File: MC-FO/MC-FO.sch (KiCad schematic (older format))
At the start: 16 parts, among them J1 86094327313755E1LF, U161 IFD97, U163 74LVC1G32SE-7

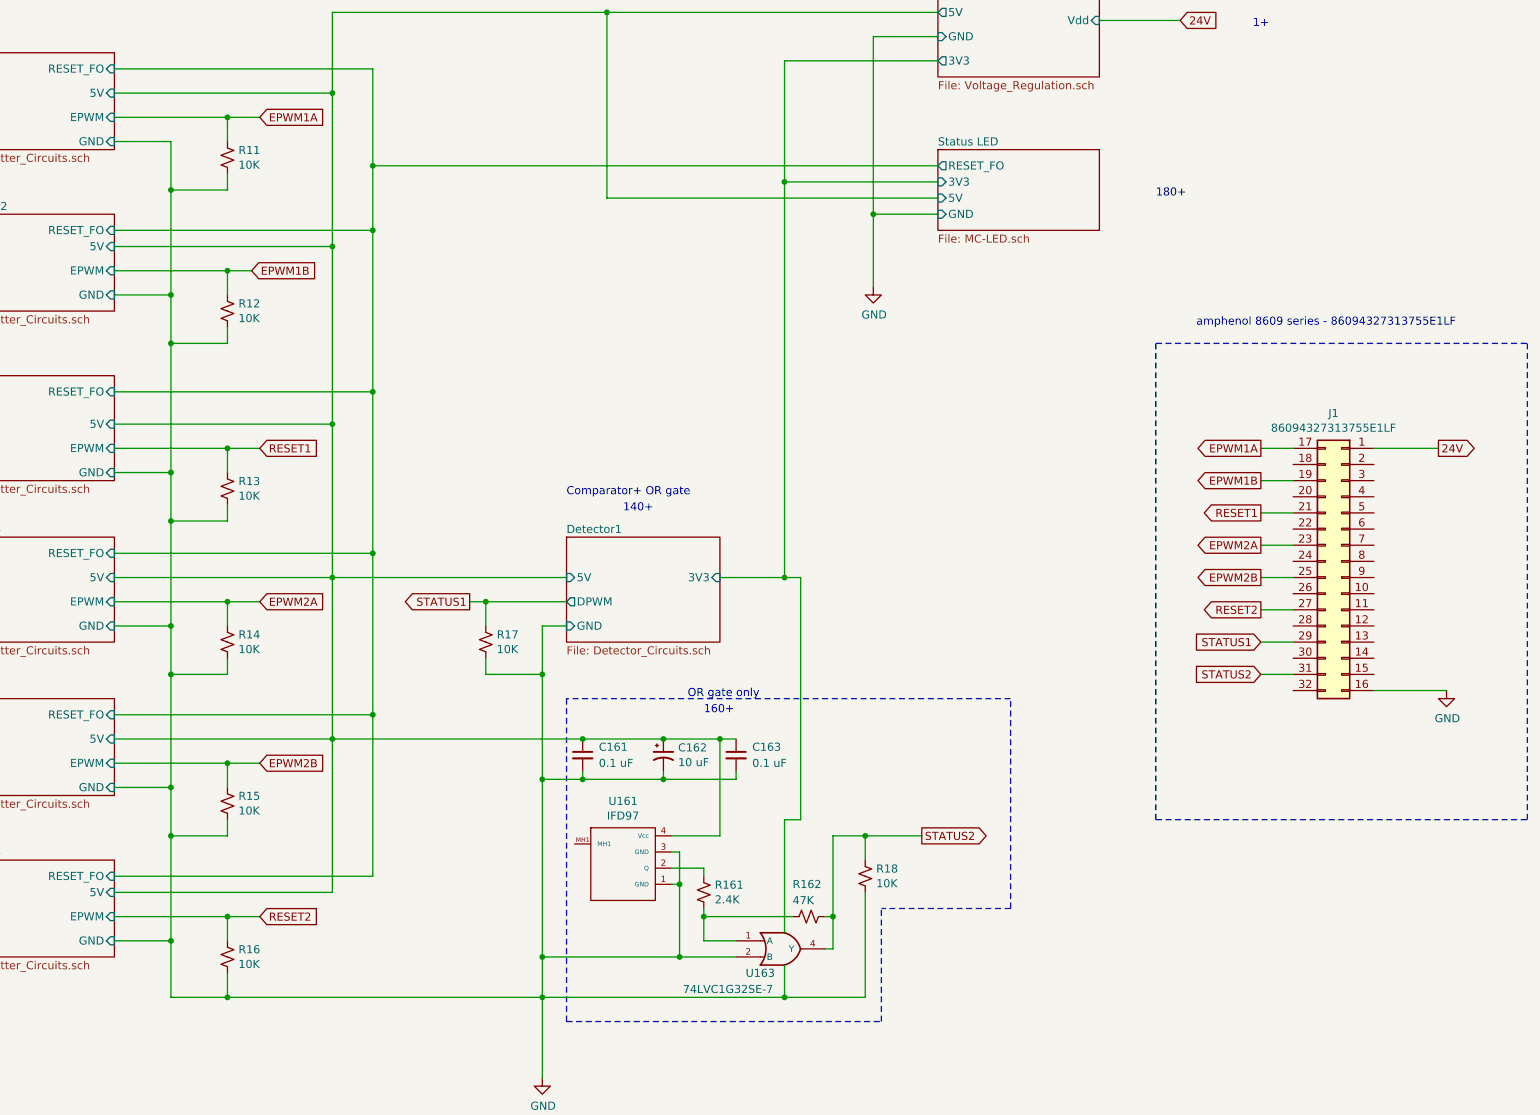
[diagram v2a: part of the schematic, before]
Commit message: DSP schem, FO schem, and FO layout changes
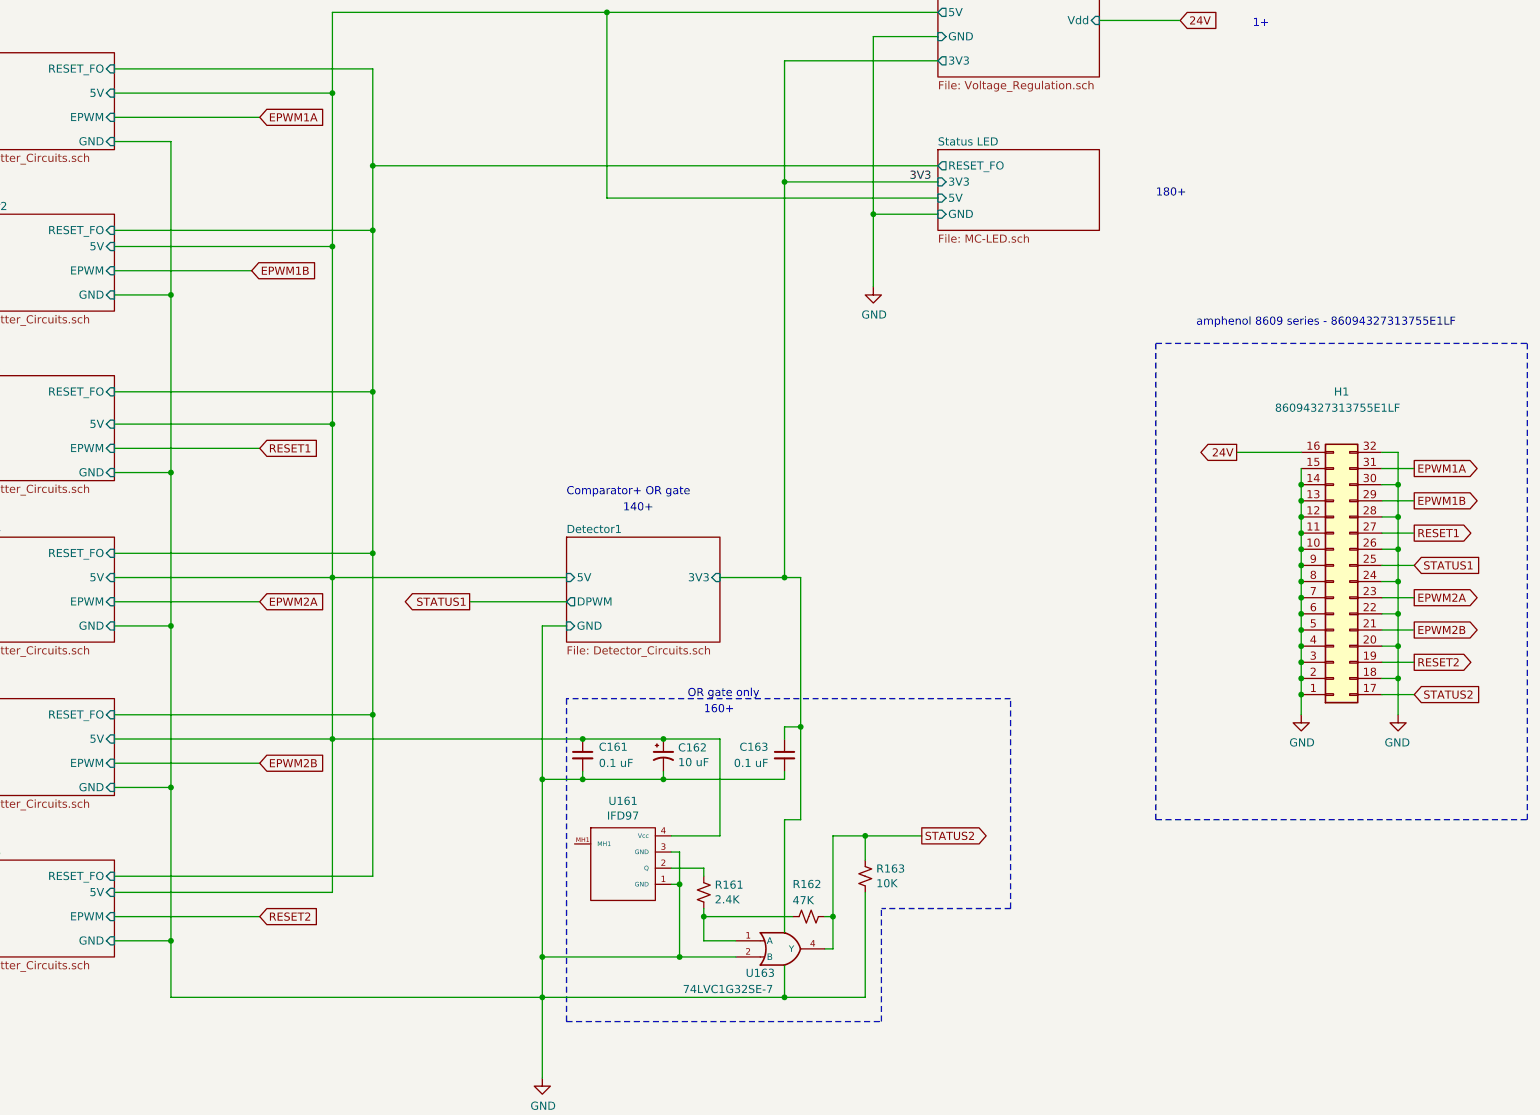
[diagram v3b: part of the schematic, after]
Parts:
- removed R11, R12, R13, R14, R15, R16, R17: 10K, Resistor_SMD:R_0603_1608Metric, symbol Device:R_Small_US
- renumbered J1 to H1, R18 to R163
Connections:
- net 24V: now also H1.16 (Pin_16); no longer H1.1 (Pin_1)
- net Detector1/5V: no longer C163.1
- net EPWM1A: now also H1.31 (Pin_31); no longer H1.17 (Pin_17)
- net EPWM1B: now also H1.29 (Pin_29); no longer H1.19 (Pin_19)
- net EPWM2B: now also H1.21 (Pin_21); no longer H1.25 (Pin_25)
- net GND: now also H1.1 (Pin_1), H1.10 (Pin_10), H1.11 (Pin_11), H1.12 (Pin_12), H1.13 (Pin_13), H1.14 (Pin_14), H1.15 (Pin_15), H1.18 (Pin_18), H1.2 (Pin_2), H1.20 (Pin_20), H1.22 (Pin_22), H1.24 (Pin_24), H1.26 (Pin_26), H1.28 (Pin_28), H1.3 (Pin_3), H1.30 (Pin_30), H1.32 (Pin_32), H1.4 (Pin_4), H1.5 (Pin_5), H1.6 (Pin_6), H1.7 (Pin_7), H1.8 (Pin_8), H1.9 (Pin_9); no longer H1.16 (Pin_16)
- net RESET1: now also H1.27 (Pin_27); no longer H1.21 (Pin_21)
- net RESET2: now also H1.19 (Pin_19); no longer H1.27 (Pin_27)
- net STATUS1: now also H1.25 (Pin_25); no longer H1.29 (Pin_29)
- net STATUS2: now also H1.17 (Pin_17); no longer H1.31 (Pin_31)
- net VCC: now also C163.1
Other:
- moved on the sheet: C163, H1

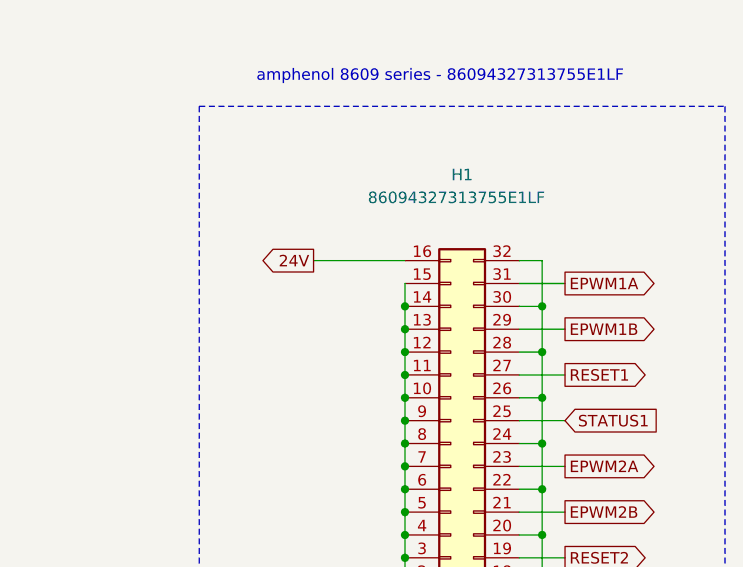
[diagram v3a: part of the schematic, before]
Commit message: Routed FO schematic
All FO circuits routed except LED and Detector circuits.
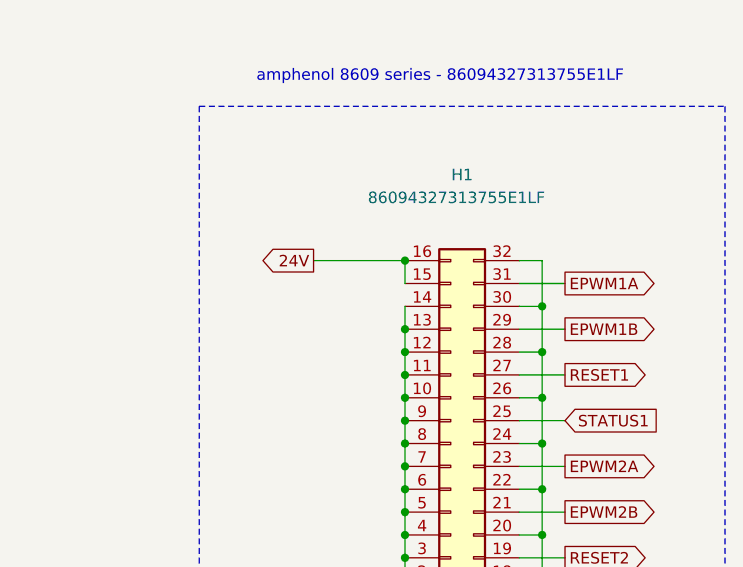
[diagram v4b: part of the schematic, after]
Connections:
- net 24V: now also H1.15 (Pin_15)
- net GND: no longer H1.15 (Pin_15)
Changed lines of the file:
@@
 EPWM1A
 Connection ~ 10000 4975
-Connection ~ 9400 4275
-Wire Wire Line
-	9400 4375 9400 4275
-Connection ~ 9400 4375
-Wire Wire Line
-	9400 4475 9400 4375
-Connection ~ 9400 4475
-Wire Wire Line
-	9400 4575 9400 4475
-Connection ~ 9400 4575
-Wire Wire Line
-	9400 4675 9400 4575
-Connection ~ 9400 4675
-Wire Wire Line
-	9400 4775 9400 4675
-Connection ~ 9400 4775
-Wire Wire Line
-	9400 4875 9400 4775
-Connection ~ 9400 4875
-Wire Wire Line
-	9400 4975 9400 4875
-Connection ~ 9400 4975
-Wire Wire Line
-	9400 3775 9400 3875
-Connection ~ 9400 3875
-Wire Wire Line
-	9400 3975 9400 3875
-Connection ~ 9400 3975
-Wire Wire Line
-	9400 4075 9400 3975
-Connection ~ 9400 4075
-Wire Wire Line
-	9400 4275 9400 4175
-Wire Wire Line
-	9400 4175 9400 4075
-Connection ~ 9400 4175
-Wire Wire Line
-	9400 5075 9400 5200
-Wire Wire Line
-	9400 4975 9400 5075
-Connection ~ 9400 5075
-$Comp
-L Existing_IC_Models:86094327313755E1LF H1
-U 1 1 61916120
-P 9600 4375
-F 0 "H1" H 9650 3200 50  0000 C CNN
-F 1 "86094327313755E1LF" H 9625 3300 50  0000 C CNN
-F 2 "Footprints_MC-FO:86094327313755E1LF" H 9600 4375 50  0001 C CNN
-F 3 "~" H 9600 4375 50  0001 C CNN
-	1    9600 4375
-	1    0    0    1
-$EndComp
-Wire Wire Line
-	9400 3775 9400 3675
-Connection ~ 9400 3775
 Wire Wire Line
 	10000 3575 9900 3575
@@
 Wire Wire Line
 	4250 4500 4850 4500
+Connection ~ 9400 4275
+Wire Wire Line
+	9400 4375 9400 4275
+Connection ~ 9400 4375
+Wire Wire Line
+	9400 4475 9400 4375
+Connection ~ 9400 4475
+Wire Wire Line
+	9400 4575 9400 4475
+Connection ~ 9400 4575
+Wire Wire Line
+	9400 4675 9400 4575
+Connection ~ 9400 4675
+Wire Wire Line
+	9400 4775 9400 4675
+Connection ~ 9400 4775
+Wire Wire Line
+	9400 4875 9400 4775
+Connection ~ 9400 4875
+Wire Wire Line
+	9400 4975 9400 4875
+Connection ~ 9400 4975
+Wire Wire Line
+	9400 3775 9400 3875
+Connection ~ 9400 3875
+Wire Wire Line
+	9400 3975 9400 3875
+Connection ~ 9400 3975
+Wire Wire Line
+	9400 4075 9400 3975
+Connection ~ 9400 4075
+Wire Wire Line
+	9400 4175 9400 4075
+Wire Wire Line
+	9400 4275 9400 4175
+Connection ~ 9400 4175
+Wire Wire Line
+	9400 4975 9400 5075
+Connection ~ 9400 5075
+Wire Wire Line
+	9400 5075 9400 5200
+$Comp
+L Existing_IC_Models:86094327313755E1LF H1
+U 1 1 61916120
+P 9600 4375
+F 0 "H1" H 9650 3200 50  0000 C CNN
+F 1 "86094327313755E1LF" H 9625 3300 50  0000 C CNN
+F 2 "Footprints_MC-FO:86094327313755E1LF" H 9600 4375 50  0001 C CNN
+F 3 "~" H 9600 4375 50  0001 C CNN
+	1    9600 4375
+	1    0    0    1
+$EndComp
+Wire Wire Line
+	9400 3675 9400 3575
+Connection ~ 9400 3575
 $EndSCHEMATC

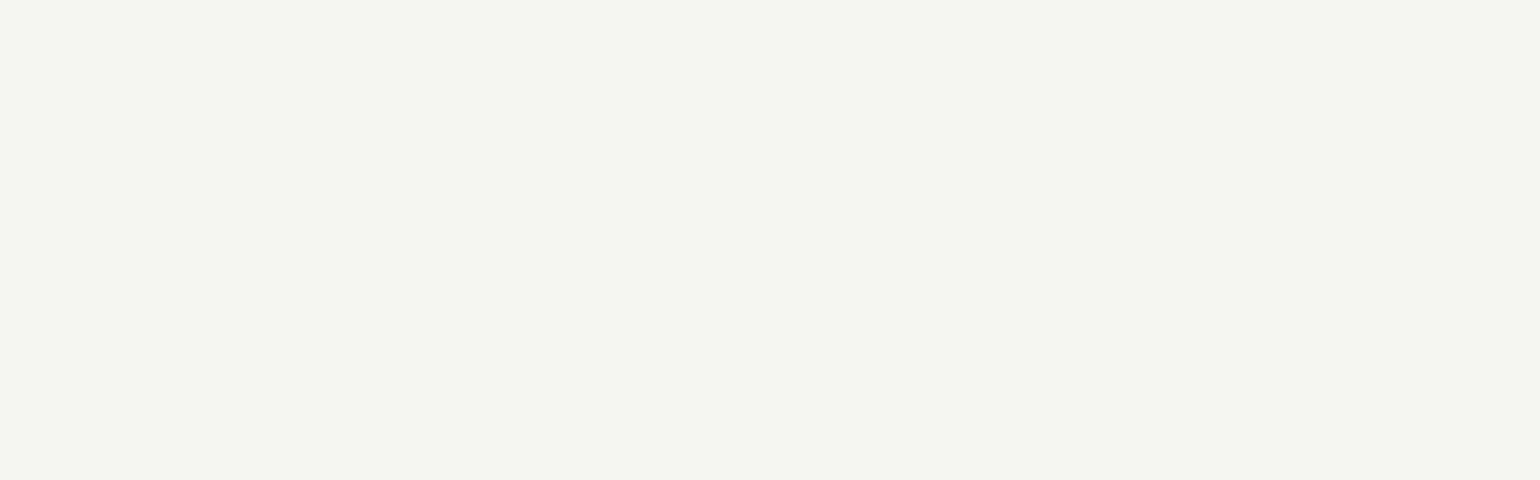
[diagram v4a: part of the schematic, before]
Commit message: updated top level of schematic with "to test" and "to do" notes
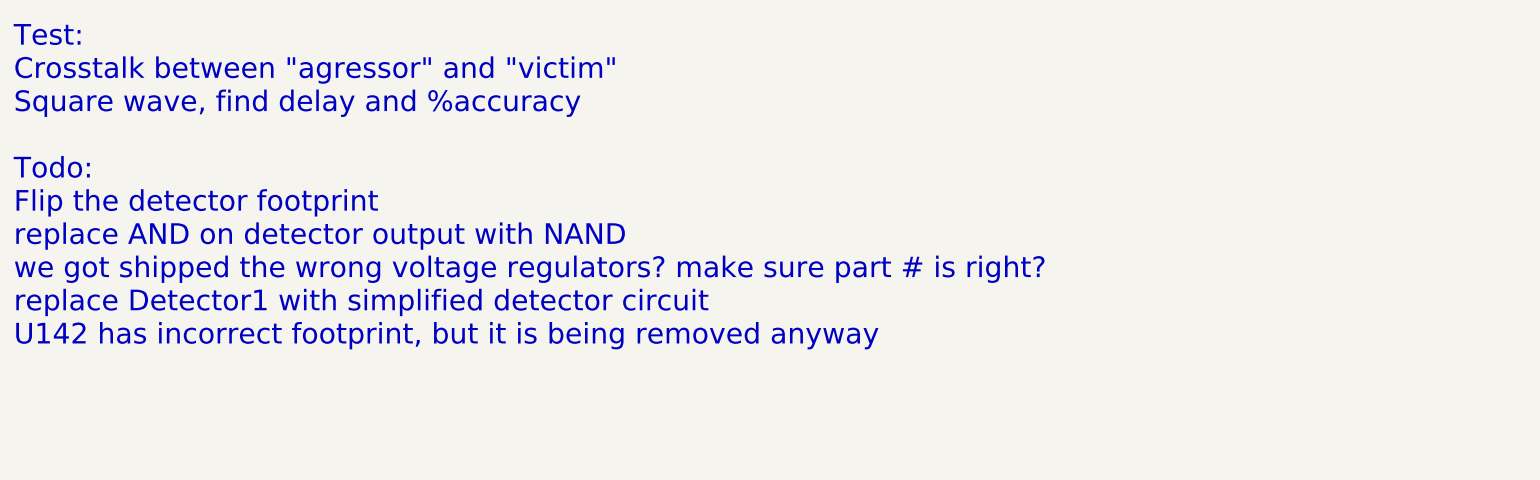
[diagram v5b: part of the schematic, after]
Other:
- note added: "Test:\nCrosstalk between "agressor" and "victim"\nSquare wave, find delay and %accuracy \n\nTodo:\nFlip the detector footprint\nreplace AND on detector output with NAND\nwe got shipped the wrong voltage regulators? make sure part # is right?\nreplace Detector1 with simplified detector circuit\nU142 has incorrect footprint, but it is being removed anyway\n"
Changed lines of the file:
@@
 	9400 3675 9400 3575
 Connection ~ 9400 3575
+Text Notes 350  -300 0    118  ~ 0
+Test:\nCrosstalk between "agressor" and "victim"\nSquare wave, find delay and %accuracy \n\nTodo:\nFlip the detector footprint\nreplace AND on detector output with NAND\nwe got shipped the wrong voltage regulators? make sure part # is right?\nreplace Detector1 with simplified detector circuit\nU142 has incorrect footprint, but it is being removed anyway\n
 $EndSCHEMATC

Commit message: ADC refs, FTDI changes, and more
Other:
- note added: "Test:\nCrosstalk between "agressor" and "victim"\nSquare wave, find delay and %accuracy \n\nTodo:\nFlip the detector footprint\nreplace AND on detector output with NAND\nwe got shipped the wrong voltage regulators? make sure part # is right?\nreplace Detector1 with simplified detector circuit\nU142 has incorrect footprint, but it is being removed anyway\nmake safe mode and FO enable control emitt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"
- note removed: "Test:\nCrosstalk between "agressor" and "victim"\nSquare wave, find delay and %accuracy \n\nTodo:\nFlip the detector footprint\nreplace AND on detector output with NAND\nwe got shipped the wrong voltage regulators? make sure part # is right?\nreplace Detector1 with simplified detector circuit\nU142 has incorrect footprint, but it is being removed anyway\n"
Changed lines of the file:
@@
 Connection ~ 9400 3575
 Text Notes 350  -300 0    118  ~ 0
-Test:\nCrosstalk between "agressor" and "victim"\nSquare wave, find delay and %accuracy \n\nTodo:\nFlip the detector footprint\nreplace AND on detector output with NAND\nwe got shipped the wrong voltage regulators? make sure part # is right?\nreplace Detector1 with simplified detector circuit\nU142 has incorrect footprint, but it is being removed anyway\n
+Test:\nCrosstalk between "agressor" and "victim"\nSquare wave, find delay and %accuracy \n\nTodo:\nFlip the detector footprint\nreplace AND on detector output with NAND\nwe got shipped the wrong voltage regulators? make sure part # is right?\nreplace Detector1 with simplified detector circuit\nU142 has incorrect footprint, but it is being removed anyway\nmake safe mode and FO enable control emitters
 $EndSCHEMATC

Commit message: Add files via upload
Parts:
- removed C161, C163: 0.1 uF, Capacitor_SMD:C_0603_1608Metric, symbol Device:C_Small
- removed C162: 10 uF, Capacitor_SMD:C_0603_1608Metric, symbol Device:CP1_Small
- removed R161: 2.4K, Resistor_SMD:R_0603_1608Metric, symbol Device:R_Small_US
- removed R162: 47K, Resistor_SMD:R_0603_1608Metric, symbol Device:R_Small_US
- removed R163: 10K, Resistor_SMD:R_0603_1608Metric, symbol Device:R_Small_US
- removed U161: IFD97, Footprints_MC-FO:IFE98, symbol Existing_IC_Models:IFD97
- removed U163: 74LVC1G32SE-7, Package_TO_SOT_SMD:SOT-353_SC-70-5, symbol Existing_IC_Models:74LVC1G32SE-7
- added TP1, TP10, TP11, TP2, TP3, TP4, TP5, TP6, TP7, TP8, TP9: TestPoint, TestPoint:TestPoint_Pad_D2.0mm, symbol Connector:TestPoint
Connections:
- net RESET2 is gone; now on net STATUS2: H1.19 (Pin_19)
- net Detector1/5V: now also TP8.1
- net EPWM1A: now also TP4.1
- net EPWM1B: now also TP2.1
- net EPWM2A: now also TP3.1
- net EPWM2B: now also TP5.1
- net GND: now also H1.17 (Pin_17); no longer H1.11 (Pin_11), H1.9 (Pin_9)
- net STATUS1: now also TP11.1
- net STATUS2: now also TP10.1; no longer H1.17 (Pin_17)
- net RESET1 renamed RESET_GPIO
- net RESET_GPIO: now also TP1.1, TP6.1
- new net 3V3: TP9.1
- new net EMITTER_ENABLE: H1.9 (Pin_9)
- new net SAFE_STATE_FLAG: H1.11 (Pin_11), TP7.1
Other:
- note added: "Test:\nCrosstalk between "agressor" and "victim"\nSquare wave, find delay and %accuracy \n\nTodo:\nFlip the detector footprint --- DONE( the pins were labelled incorrectly in the schematic)\nreplace AND on detector output with NAND------ DONE (decided to use NOR instead\nwe got shipped the wrong voltage regulators? make sure part # is right? --- corrrect schematic (mouser error)\nreplace Detector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"
- note removed: "Comparator+ OR gate"
- note removed: "OR gate only"
- note removed: "Test:\nCrosstalk between "agressor" and "victim"\nSquare wave, find delay and %accuracy \n\nTodo:\nFlip the detector footprint\nreplace AND on detector output with NAND\nwe got shipped the wrong voltage regulators? make sure part # is right?\nreplace Detector1 with simplified detector circuit\nU142 has incorrect footprint, but it is being removed anyway\nmake safe mode and FO enable control emitt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"
- moved on the sheet: H1
